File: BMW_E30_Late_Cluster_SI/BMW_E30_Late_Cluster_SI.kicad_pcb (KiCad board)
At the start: 2 copper layers, 78.7 x 3.1 mm, 12 parts, among them J1 SI LED Board, J5 Nexus Connector, Y1 Crystal, Y2 Crystal

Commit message: SI Board Cuts
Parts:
- moved J5 116.7 mm to (221.5, 133.5)
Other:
- board size 78.7 x 3.1 mm -> 300 x 53 mm
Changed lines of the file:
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@@
 	(footprint "BMW_Cluster_Connectors:E30_SI_Connector_Late_19Pin_P3.5"
 		(layer "F.Cu")
-		(at 272.5 28.5)
+		(at 221.5 133.5)
 		(property "Reference" "J5"
 			(at 35.835 3.875 0)
@@
 		)
 	)
+	(gr_line
+		(start 149.4 183)
+		(end 70 183)
+		(stroke
+			(width 0.05)
+			(type solid)
+		)
+		(layer "Edge.Cuts")
+	)
+	(gr_line
+		(start 70 130)
+		(end 70 183)
+		(stroke
+			(width 0.05)
+			(type default)
+		)
+		(layer "Edge.Cuts")
+	)
+	(gr_line
+		(start 289.4 175.7)
+		(end 264.5 175.7)
+		(stroke
+			(width 0.05)
+			(type solid)
+		)
+		(layer "Edge.Cuts")
+	)
+	(gr_line
+		(start 342 155.5)
+		(end 317 155.5)
+		(stroke
+			(width 0.05)
+			(type solid)
+		)
+		(layer "Edge.Cuts")
+	)
+	(gr_line
+		(start 70 130)
+		(end 370 130)
+		(stroke
+			(width 0.05)
+			(type solid)
+		)
+		(layer "Edge.Cuts")
+	)
+	(gr_line
+		(start 174.3 183)
+		(end 174.3 175.7)
+		(stroke
+			(width 0.05)
+			(type solid)
+		)
+		(layer "Edge.Cuts")
+	)
+	(gr_line
+		(start 264.5 183)
+		(end 174.3 183)
+		(stroke
+			(width 0.05)
+			(type solid)
+		)
+		(layer "Edge.Cuts")
+	)
+	(gr_line
+		(start 370 146.9)
+		(end 342 146.9)
+		(stroke
+			(width 0.05)
+			(type solid)
+		)
+		(layer "Edge.Cuts")
+	)
+	(gr_line
+		(start 149.4 183)
+		(end 149.4 175.7)
+		(stroke
+			(width 0.05)
+			(type solid)
+		)
+		(layer "Edge.Cuts")
+	)
+	(gr_line
+		(start 289.4 183)
+		(end 289.4 175.7)
+		(stroke
+			(width 0.05)
+			(type solid)
+		)
+		(layer "Edge.Cuts")
+	)
+	(gr_line
+		(start 370 130)
+		(end 370 146.9)
+		(stroke
+			(width 0.05)
+			(type solid)
+		)
+		(layer "Edge.Cuts")
+	)
+	(gr_line
+		(start 264.5 183)
+		(end 264.5 175.7)
+		(stroke
+			(width 0.05)
+			(type solid)
+		)
+		(layer "Edge.Cuts")
+	)
+	(gr_line
+		(start 310.1 179.2)
+		(end 306.1 179.2)
+		(stroke
+			(width 0.05)
+			(type solid)
+		)
+		(layer "Edge.Cuts")
+	)
+	(gr_line
+		(start 306.1 183)
+		(end 289.4 183)
+		(stroke
+			(width 0.05)
+			(type solid)
+		)
+		(layer "Edge.Cuts")
+	)
+	(gr_line
+		(start 310.1 146.9)
+		(end 310.1 179.2)
+		(stroke
+			(width 0.05)
+			(type solid)
+		)
+		(layer "Edge.Cuts")
+	)
+	(gr_line
+		(start 342 146.9)
+		(end 342 155.5)
+		(stroke
+			(width 0.05)
+			(type default)
+		)
+		(layer "Edge.Cuts")
+	)
+	(gr_line
+		(start 317 146.9)
+		(end 317 155.5)
+		(stroke
+			(width 0.05)
+			(type default)
+		)
+		(layer "Edge.Cuts")
+	)
+	(gr_line
+		(start 174.3 175.7)
+		(end 149.4 175.7)
+		(stroke
+			(width 0.05)
+			(type solid)
+		)
+		(layer "Edge.Cuts")
+	)
+	(gr_line
+		(start 306.1 179.2)
+		(end 306.1 183)
+		(stroke
+			(width 0.05)
+			(type solid)
+		)
+		(layer "Edge.Cuts")
+	)
+	(gr_line
+		(start 317 146.9)
+		(end 310.1 146.9)
+		(stroke
+			(width 0.05)
+			(type solid)
+		)
+		(layer "Edge.Cuts")
+	)
 	(embedded_fonts no)

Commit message: SI layout updates
Component positions are mostly complete.
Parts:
- added BT1: 3V, SI_THT:Batt_CR14250SE, F.Cu at (236.5, 155.9)
- added BT2: 3V, SI_THT:Batt_CR14250SE, F.Cu at (236.5, 142.3)
- added C1: 0.1u, Capacitor_THT:C_Disc_D6.0mm_W2.5mm_P5.00mm, F.Cu at (281.9, 114.3)
- added C10: 68n, Capacitor_THT:C_Disc_D6.0mm_W2.5mm_P5.00mm, F.Cu at (272.4, 120.2)
- added C13: 47u, Capacitor_THT:CP_Radial_Tantal_D9.0mm_P2.50mm, F.Cu at (90.1, 175.8)
- added C14: 10n, Capacitor_THT:C_Disc_D6.0mm_W2.5mm_P5.00mm, F.Cu at (127.7, 179.9)
- added C17: 68n, Capacitor_THT:C_Disc_D6.0mm_W2.5mm_P5.00mm, F.Cu at (163.3, 164.6)
- added C18: 0.1u, Capacitor_THT:C_Rect_L7.0mm_W2.0mm_P5.00mm, F.Cu at (219.5, 141.4)
- added C19: 0.1n, Capacitor_THT:C_Disc_D6.0mm_W2.5mm_P5.00mm, F.Cu at (210.6, 149.3)
- added C20: 0.1n, Capacitor_THT:C_Disc_D6.0mm_W2.5mm_P5.00mm, F.Cu at (219.8, 146.1)
- added C21: 0.1n, Capacitor_THT:C_Disc_D6.0mm_W2.5mm_P5.00mm, F.Cu at (85.0, 156.5)
- added C3: 0.1u, Capacitor_THT:C_Disc_D6.0mm_W2.5mm_P5.00mm, F.Cu at (281.9, 118.3)
- added C5: 0.1u, Capacitor_THT:C_Rect_L7.0mm_W2.0mm_P5.00mm, F.Cu at (293.9, 153.7)
- added C6: 0.033u, Capacitor_THT:C_Rect_L7.0mm_W2.0mm_P5.00mm, F.Cu at (238.7, 52.4)
- added C7: 10n, Capacitor_THT:C_Rect_L7.0mm_W2.0mm_P5.00mm, F.Cu at (238.7, 55.9)
- added C8: 47n, Capacitor_THT:C_Disc_D6.0mm_W2.5mm_P5.00mm, F.Cu at (272.4, 116.1)
- added C9: 68n, Capacitor_THT:C_Disc_D6.0mm_W2.5mm_P5.00mm, F.Cu at (281.9, 122.4)
- added D1: 1N4004, SI_THT:D_Axial_Narrow_L6.7mm_D2.4mm_P9.7mm, F.Cu at (262.0, 160.3)
- added D10: BZX55C-5V1, SI_THT:D_Axial_Narrow_L6.7mm_D2.4mm_P9.7mm, F.Cu at (187.2, 43.5)
- added D16: BZX55C-9V1, SI_THT:D_Axial_Narrow_L6.7mm_D2.4mm_P9.7mm, F.Cu at (79.6, 170.6)
- added D18: 1N4148, SI_THT:D_Axial_Narrow_L6.7mm_D2.4mm_P9.7mm, F.Cu at (187.2, 103.1)
- added D2: BAV21, SI_THT:D_Axial_Narrow_L6.7mm_D2.4mm_P9.7mm, F.Cu at (254.7, 41.9)
- added D24: SD103A, SI_THT:D_Axial_Narrow_L6.7mm_D2.4mm_P9.7mm, F.Cu at (214.3, 146.1)
- added D25: SD103A, SI_THT:D_Axial_Narrow_L6.7mm_D2.4mm_P9.7mm, F.Cu at (216.8, 146.1)
- added D26: LED, LED_THT:LED_D3.0mm, F.Cu at (90.7, 156.6)
- added D3: BAV21, SI_THT:D_Axial_Narrow_L6.7mm_D2.4mm_P9.7mm, F.Cu at (254.7, 45.5)
- added D4: 1N4004, SI_THT:D_Axial_Narrow_L6.7mm_D2.4mm_P9.7mm, F.Cu at (254.7, 49.1)
- added D5: BZX55C-5V1, SI_THT:D_Axial_Narrow_L6.7mm_D2.4mm_P9.7mm, F.Cu at (187.2, 32.7)
- added D6: BAV21, SI_THT:D_Axial_Narrow_L6.7mm_D2.4mm_P9.7mm, F.Cu at (94.6, 132.2)
- added D7: BZX55C-4V7, SI_THT:D_Axial_Narrow_L6.7mm_D2.4mm_P9.7mm, F.Cu at (87.1, 141.9)
- added D8: ZW 4.7, SI_THT:D_Axial_Narrow_L6.7mm_D2.4mm_P9.7mm, F.Cu at (245.7, 71.0)
- added D9: BAV21, SI_THT:D_Axial_Narrow_L6.7mm_D2.4mm_P9.7mm, F.Cu at (97.1, 141.9)
- added J2: Coding Plug, Connector_PinSocket_2.54mm:PinSocket_1x08_P2.54mm_Horizontal, F.Cu at (320.7, 142.1)
- added JP1: Battery Jumper, Connector_PinHeader_2.54mm:PinHeader_1x03_P2.54mm_Vertical, F.Cu at (206.0, 153.5)
- added Q11: BC327-16, Package_TO_SOT_THT:TO-92_Inline_Wide, F.Cu at (74.6, 146.4)
- added Q12: BC337-25, Package_TO_SOT_THT:TO-92_Inline_Wide, F.Cu at (79.6, 146.4)
- added Q13: BC337-16, Package_TO_SOT_THT:TO-92_Inline_Wide, F.Cu at (261.8, 136.0)
- added Q14: BC547B, Package_TO_SOT_THT:TO-92_Inline_Wide, F.Cu at (107.0, 176.7)
- added Q15: BC557B, Package_TO_SOT_THT:TO-92_Inline_Wide, F.Cu at (74.6, 173.1)
- added Q17: BC337-25, Package_TO_SOT_THT:TO-92_Inline_Wide, F.Cu at (79.6, 173.1)
- added Q19: BC337-25, Package_TO_SOT_THT:TO-92_Inline_Wide, F.Cu at (269.2, 168.2)
- added Q21: BC337-25, Package_TO_SOT_THT:TO-92_Inline_Wide, F.Cu at (261.5, 171.1)
- added Q22: BC337-25, Package_TO_SOT_THT:TO-92_Inline_Wide, F.Cu at (251.9, 171.1)
- added Q23: BC337-25, Package_TO_SOT_THT:TO-92_Inline_Wide, F.Cu at (256.7, 171.1)
- added R1: 2R2, SI_THT:R_Axial_Narrow_L6.8mm_D2.4mm_P9.7mm, F.Cu at (187.2, 47.1)
- added R10: 2k2, SI_THT:R_Axial_Narrow_L6.8mm_D2.4mm_P9.7mm, F.Cu at (82.1, 132.2)
- added R11: 2k21, SI_THT:R_Axial_Narrow_L6.8mm_D2.4mm_P9.7mm, F.Cu at (187.2, 65.1)
- added R12: 10k, SI_THT:R_Axial_Narrow_L6.8mm_D2.4mm_P9.7mm, F.Cu at (187.2, 68.7)
- added R13: 27k4, SI_THT:R_Axial_Narrow_L6.8mm_D2.4mm_P9.7mm, F.Cu at (187.2, 72.3)
- added R14: 47k, SI_THT:R_Axial_Narrow_L6.8mm_D2.4mm_P9.7mm, F.Cu at (92.1, 132.2)
- added R15: 47k, SI_THT:R_Axial_Narrow_L6.8mm_D2.4mm_P9.7mm, F.Cu at (89.6, 132.2)
- added R16: 1k5, SI_THT:R_Axial_Narrow_L6.8mm_D2.4mm_P9.7mm, F.Cu at (250.1, 114.5)
- added R17: 27k, SI_THT:R_Axial_Narrow_L6.8mm_D2.4mm_P9.7mm, F.Cu at (245.7, 96.2)
- added R18: 1k5, SI_THT:R_Axial_Narrow_L6.8mm_D2.4mm_P9.7mm, F.Cu at (245.7, 99.8)
- added R19: 470, SI_THT:R_Axial_Narrow_L6.8mm_D2.4mm_P9.7mm, F.Cu at (187.2, 83.1)
- added R2: 15k, SI_THT:R_Axial_Narrow_L6.8mm_D2.4mm_P9.7mm, F.Cu at (187.2, 50.7)
- added R21: 10k, SI_THT:R_Axial_Narrow_L6.8mm_D2.4mm_P9.7mm, F.Cu at (87.1, 160.8)
- added R22: 16k, SI_THT:R_Axial_Narrow_L6.8mm_D2.4mm_P9.7mm, F.Cu at (92.1, 160.8)
- added R23: 39k, SI_THT:R_Axial_Narrow_L6.8mm_D2.4mm_P9.7mm, F.Cu at (77.1, 160.8)
- added R24: 51k, SI_THT:R_Axial_Narrow_L6.8mm_D2.4mm_P9.7mm, F.Cu at (84.6, 160.8)
- added R25: 100R, SI_THT:R_Axial_Narrow_L6.8mm_D2.4mm_P9.7mm, F.Cu at (89.6, 170.6)
- added R26: 1k, SI_THT:R_Axial_Narrow_L6.8mm_D2.4mm_P9.7mm, F.Cu at (74.6, 170.6)
- added R28: 200R, SI_THT:R_Axial_Narrow_L6.8mm_D2.4mm_P9.7mm, F.Cu at (82.1, 170.6)
- added R29: 100k, SI_THT:R_Axial_Narrow_L6.8mm_D2.4mm_P9.7mm, F.Cu at (187.2, 113.9)
- added R3: 2R2, SI_THT:R_Axial_Narrow_L6.8mm_D2.4mm_P9.7mm, F.Cu at (187.2, 54.3)
- added R30: 75R, SI_THT:R_Axial_Narrow_L6.8mm_D2.4mm_P9.7mm, F.Cu at (187.2, 117.5)
- added R32: 160R, SI_THT:R_Axial_Narrow_L6.8mm_D2.4mm_P9.7mm, F.Cu at (188.2, 171.2)
- added R33: 160R, SI_THT:R_Axial_Narrow_L6.8mm_D2.4mm_P9.7mm, F.Cu at (190.7, 171.2)
- added R34: 160R, SI_THT:R_Axial_Narrow_L6.8mm_D2.4mm_P9.7mm, F.Cu at (193.2, 171.2)
- added R35: 160R, SI_THT:R_Axial_Narrow_L6.8mm_D2.4mm_P9.7mm, F.Cu at (200.7, 171.2)
- added R36: 160R, SI_THT:R_Axial_Narrow_L6.8mm_D2.4mm_P9.7mm, F.Cu at (198.2, 171.2)
- added R37: 160R, SI_THT:R_Axial_Narrow_L6.8mm_D2.4mm_P9.7mm, F.Cu at (203.2, 171.2)
- added R38: 160R, SI_THT:R_Axial_Narrow_L6.8mm_D2.4mm_P9.7mm, F.Cu at (205.7, 171.2)
- added R39: 4k7, SI_THT:R_Axial_Narrow_L6.8mm_D2.4mm_P9.7mm, F.Cu at (239.0, 180.8)
- added R4: 6k8, SI_THT:R_Axial_Narrow_L6.8mm_D2.4mm_P9.7mm, F.Cu at (74.6, 141.9)
- added R40: 4k7, SI_THT:R_Axial_Narrow_L6.8mm_D2.4mm_P9.7mm, F.Cu at (241.5, 180.8)
- added R41: 4k7, SI_THT:R_Axial_Narrow_L6.8mm_D2.4mm_P9.7mm, F.Cu at (247.4, 180.8)
- added R42: 82R, SI_THT:R_Axial_Narrow_L6.8mm_D2.4mm_P9.7mm, F.Cu at (196.4, 139.6)
- added R43: 82R, SI_THT:R_Axial_Narrow_L6.8mm_D2.4mm_P9.7mm, F.Cu at (193.9, 139.6)
- added R44: 2k, SI_THT:R_Axial_Narrow_L6.8mm_D2.4mm_P9.7mm, F.Cu at (162.1, 142.8)
- added R45: 1M, SI_THT:R_Axial_Narrow_L6.8mm_D2.4mm_P9.7mm, F.Cu at (180.6, 164.5)
- added R46: 100R, SI_THT:R_Axial_Narrow_L6.8mm_D2.4mm_P9.7mm, F.Cu at (92.0, 153.0)
- added R5: 4k6, SI_THT:R_Axial_Narrow_L6.8mm_D2.4mm_P9.7mm, F.Cu at (77.1, 132.2)
- added R7: 27k, SI_THT:R_Axial_Narrow_L6.8mm_D2.4mm_P9.7mm, F.Cu at (187.2, 57.9)
- added R8: 3k92, SI_THT:R_Axial_Narrow_L6.8mm_D2.4mm_P9.7mm, F.Cu at (187.2, 61.5)
- added R9: 4k6, SI_THT:R_Axial_Narrow_L6.8mm_D2.4mm_P9.7mm, F.Cu at (79.6, 132.2)
- added U1: ITT SAF1190-196 MCU, Package_DIP:DIP-40_W15.24mm_LongPads, F.Cu at (99.8, 151.4)
- added U2: ITT V3003-393, Package_DIP:DIP-18_W7.62mm_LongPads, F.Cu at (175.9, 132.6)
- added U3: ITT V3004-520, Package_DIP:DIP-24_W15.24mm_LongPads, F.Cu at (163.3, 160.7)
- added U4: ITT SAF1194-280 MCU, Package_DIP:DIP-40_W15.24mm_LongPads, F.Cu at (99.8, 171.1)
- added U5: LP2950-5.0_TO92, Package_TO_SOT_THT:TO-92_Inline_Wide, F.Cu at (292.1, 142.9)
- J5: footprint BMW_Cluster_Connectors:E30_SI_Connector_Late_19Pin_P3.5 -> BMW_Cluster_Connectors:E30_Early_SI_Conn_Late_P3.5
- moved C11 282.1 mm to (100.1, 176.5), turned to -90 degrees
- moved Y2 278.5 mm to (115.0, 176.4), turned to 90 degrees
- moved R20 195.5 mm to (151.2, 162.7), turned to 90 degrees
- moved Y1 194.6 mm to (195.8, 161.9), turned to 90 degrees
- moved C12 156.8 mm to (209.9, 175.8)
- moved C15 144.4 mm to (302.9, 140.2)
- moved R6 138.6 mm to (298.7, 132.9)
- moved J1 131.4 mm to (234.6, 168.6), turned to -90 degrees
- moved C4 119.2 mm to (274.8, 170.9)
- moved R27 94.6 mm to (304.2, 155.7), turned to -90 degrees
- moved C2 86.6 mm to (294.5, 136.0), turned to 180 degrees
- moved J5 1.50 mm to (220.6, 132.3)
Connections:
- C11 pad 1: unconnected-(C11-Pad1) -> Net-(C11-Pad1)
- C11 pad 2: unconnected-(C11-Pad2) -> GNDPWR
- C12 pad 1: unconnected-(C12-Pad1) -> Net-(Q17-C)
- C12 pad 2: unconnected-(C12-Pad2) -> GNDPWR
- C15 pad 1: unconnected-(C15-Pad1) -> +5V
- C15 pad 2: unconnected-(C15-Pad2) -> GNDPWR
- C2 pad 1: unconnected-(C2-Pad1) -> VCC_T30
- C2 pad 2: unconnected-(C2-Pad2) -> GNDPWR
- C4 pad 1: unconnected-(C4-Pad1) -> VCC_T15
- C4 pad 2: unconnected-(C4-Pad2) -> GNDPWR
- J1 pad 1: unconnected-(J1-Pin_1-Pad1) -> VCC_T15
- J1 pad 10: unconnected-(J1-Pin_10-Pad10) -> Net-(J1-Pin_10)
- J1 pad 11: unconnected-(J1-Pin_11-Pad11) -> Net-(J1-Pin_11)
- J1 pad 12: unconnected-(J1-Pin_12-Pad12) -> Net-(J1-Pin_12)
- J1 pad 2: unconnected-(J1-Pin_2-Pad2) -> Net-(J1-Pin_2)
- J1 pad 3: unconnected-(J1-Pin_3-Pad3) -> Net-(J1-Pin_3)
- J1 pad 4: unconnected-(J1-Pin_4-Pad4) -> Net-(J1-Pin_4)
- J1 pad 5: unconnected-(J1-Pin_5-Pad5) -> Net-(J1-Pin_5)
- J1 pad 6: unconnected-(J1-Pin_6-Pad6) -> Net-(J1-Pin_6)
- J1 pad 7: unconnected-(J1-Pin_7-Pad7) -> Net-(J1-Pin_7)
- J1 pad 8: unconnected-(J1-Pin_8-Pad8) -> Net-(J1-Pin_8)
- J1 pad 9: unconnected-(J1-Pin_9-Pad9) -> Net-(J1-Pin_9)
- R20 pad 1: unconnected-(R20-Pad1) -> IC3_P7
- R20 pad 2: unconnected-(R20-Pad2) -> IC1_P23
- R27 pad 1: unconnected-(R27-Pad1) -> T30_Protected
- R27 pad 2: unconnected-(R27-Pad2) -> Net-(Q17-C)
- R6 pad 2: unconnected-(R6-Pad2) -> Net-(Q11-C)
- Y1 pad 1: unconnected-(Y1-Pad1) -> IC2_P12
- Y1 pad 2: unconnected-(Y1-Pad2) -> IC2_P11
- Y2 pad 1: unconnected-(Y2-Pad1) -> Net-(U4-Pad6)
- Y2 pad 2: unconnected-(Y2-Pad2) -> Net-(U4-Pad7)
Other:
- outline, holes or cut-outs redrawn

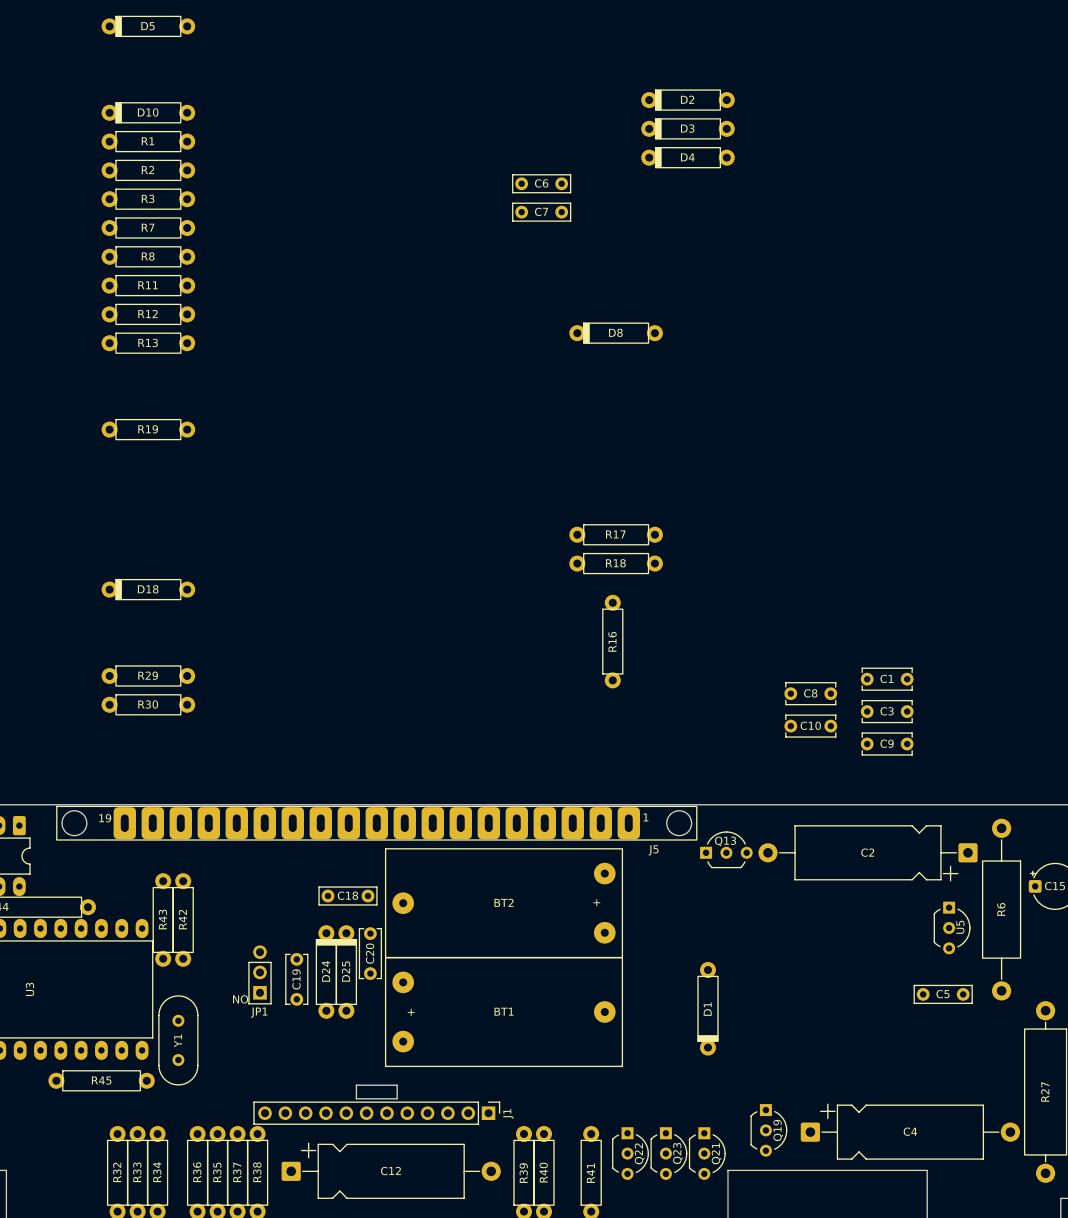
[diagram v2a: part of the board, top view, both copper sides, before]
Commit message: Component Locations Generally Set
Component locations set up and ready for layout to begin.
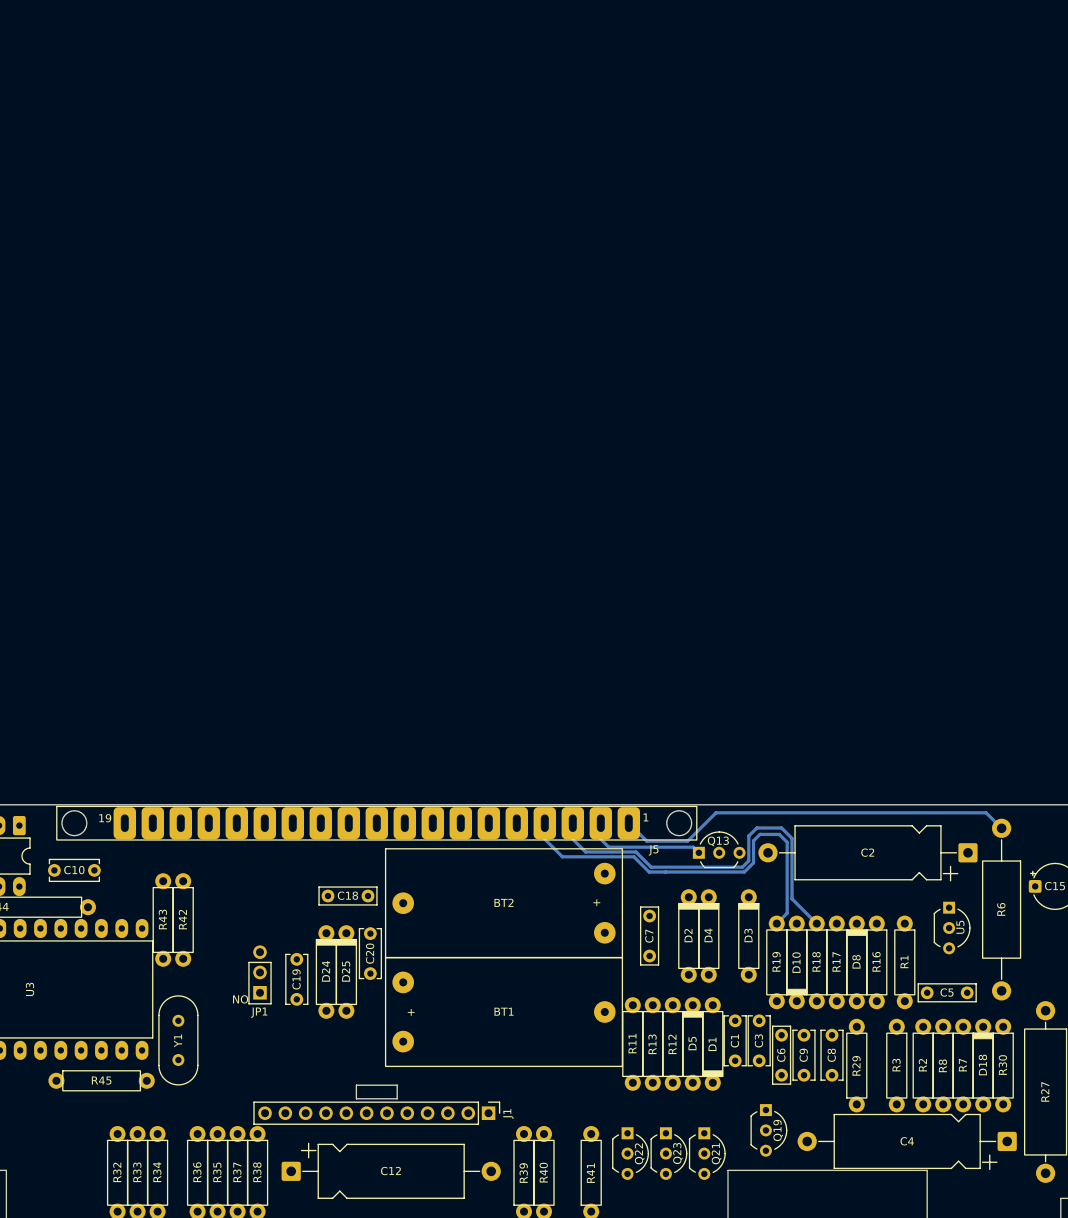
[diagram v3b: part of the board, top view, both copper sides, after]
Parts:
- moved R8 148.6 mm to (291.4, 167.4), turned to 90 degrees
- moved R2 147.7 mm to (288.9, 157.8), turned to -90 degrees
- moved R7 146.1 mm to (293.9, 157.8), turned to -90 degrees
- moved R3 142.8 mm to (285.6, 157.8), turned to -90 degrees
- moved D5 142.4 mm to (260.1, 155.1), turned to -90 degrees
- moved D10 140.4 mm to (273.1, 154.6), turned to 90 degrees
- moved R1 139.4 mm to (286.6, 144.8), turned to -90 degrees
- moved D18 122.1 mm to (296.4, 157.8), turned to -90 degrees
- moved R12 119.1 mm to (257.6, 164.8), turned to 90 degrees
- moved R30 118.7 mm to (298.9, 157.8), turned to -90 degrees
- moved R13 114.7 mm to (255.1, 164.8), turned to 90 degrees
- moved C6 111.3 mm to (271.2, 158.8), turned to -90 degrees
- moved R11 111.2 mm to (252.6, 155.1), turned to -90 degrees
- moved R29 107.7 mm to (280.6, 167.4), turned to 90 degrees
- moved R19 103.8 mm to (270.6, 144.8), turned to -90 degrees
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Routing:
- net Temp_+Ub: track 0.00 -> 49.8 mm
- net SI_RST: track 0.00 -> 48.7 mm
- net Eng_temp_sensor: track 0.00 -> 47.2 mm
- net Temp_GND: track 0.00 -> 15.0 mm

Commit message: SI Board Layout Updates
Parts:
- moved U5 1.34 mm to (290.8, 142.9)
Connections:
- net T30_Protected renamed Net-(D1-K)
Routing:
- net Net-(Q11-C): track 0.00 -> 273.5 mm, vias 0 -> 1
- net Net-(Q13-B): track 0.00 -> 235.4 mm, vias 0 -> 1
- net GNDPWR: track 0.00 -> 196.2 mm
- net +5V: track 0.00 -> 104.1 mm, vias 0 -> 2
- net Net-(Q19-C): track 0.00 -> 102.9 mm
- net Net-(D1-K): track 0.00 -> 68.0 mm
- net +12_T30: track 0.00 -> 62.6 mm, vias 0 -> 2
- net +12_T15: track 0.00 -> 56.2 mm, vias 0 -> 2
- net Net-(D2-K): track 0.00 -> 42.7 mm
- net Net-(Q17-C): track 0.00 -> 42.0 mm
- net IGN_Check: track 0.00 -> 41.1 mm, vias 0 -> 2
- net VCC_T15: track 0.00 -> 20.8 mm, vias 0 -> 1
- net VCC_T30: track 0.00 -> 20.4 mm
- net Net-(D5-A): track 0.00 -> 15.8 mm
- net IC1_P22: track 0.00 -> 9.85 mm
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- added copper zone on B.Cu, net GNDPWR

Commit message: SI Board Layout Updates
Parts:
- R20: footprint Resistor_THT:R_Axial_DIN0207_L6.3mm_D2.5mm_P15.24mm_Horizontal -> SI_THT:R_Axial_DIN0207_L6.3mm_D2.5mm_P22.2mm_Horizontal
- R44: footprint SI_THT:R_Axial_Narrow_L6.8mm_D2.4mm_P9.7mm -> SI_THT:R_Axial_Narrow_L6.8mm_D2.4mm_P22.4mm
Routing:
- net VCC_T15: track 20.8 -> 413.6 mm, vias 1 -> 3
- net IC1_P17: track 0.00 -> 87.6 mm, vias 0 -> 1
- net Net-(C14-Pad1): track 0.00 -> 73.3 mm, vias 0 -> 1
- net Net-(C6-Pad1): track 0.00 -> 21.1 mm
- net GNDPWR: track 196.2 -> 215.9 mm, vias 0 -> 1
- net IC1_P19: track 0.00 -> 11.6 mm, vias 0 -> 1
- net IC4_P40: track 0.00 -> 7.12 mm
- net Net-(R2-Pad2): track 0.00 -> 5.00 mm

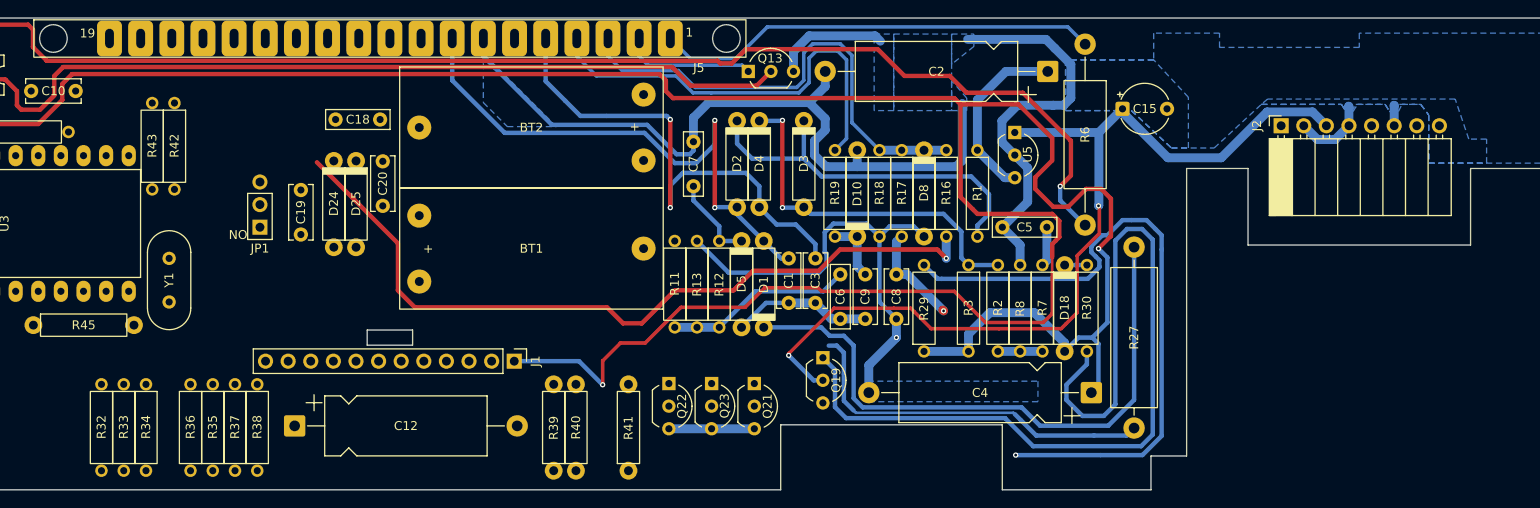
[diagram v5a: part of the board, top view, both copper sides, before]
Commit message: SI Board Layout Updates
Continued updating traces from the coding plug side of the board.
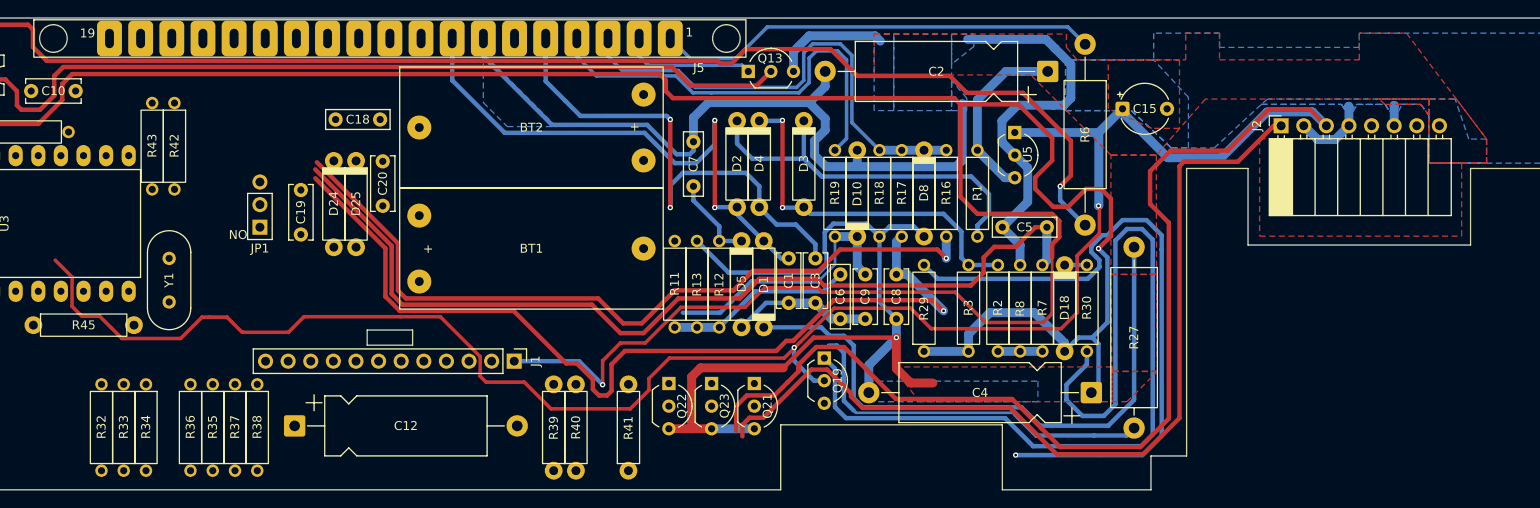
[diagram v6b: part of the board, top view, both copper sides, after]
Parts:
- moved Q19 0.16 mm to (269.4, 168.2)
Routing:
- net +5V: track 104.1 -> 316.7 mm
- net IC1_P2: track 0.00 -> 100.4 mm
- net IC1_P20: track 4.46 -> 104.0 mm
- net IC1_P19: track 11.6 -> 102.7 mm
- net GNDPWR: track 215.9 -> 254.8 mm
- net IC4_P40: track 7.12 -> 29.6 mm
- added copper zone on F.Cu, net GNDPWR

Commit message: SI Board Layout Updates
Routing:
- net Net-(C14-Pad1): track 73.3 -> 305.3 mm, vias 1 -> 3
- net IC1_P4: track 0.00 -> 144.1 mm
- net IC1_P3: track 0.00 -> 140.3 mm
- net +5V: track 316.7 -> 204.1 mm
- net Net-(Q17-C): track 42.0 -> 127.4 mm, vias 0 -> 1
- net Net-(D1-K): track 68.0 -> 130.9 mm, vias 0 -> 1
- net Net-(J1-Pin_11): track 0.00 -> 62.3 mm
- net Net-(J1-Pin_10): track 0.00 -> 51.2 mm
- net Net-(J1-Pin_2): track 0.00 -> 49.9 mm
- net Net-(J1-Pin_9): track 0.00 -> 44.7 mm
- net Net-(Q21-B): track 0.00 -> 37.6 mm
- net IC4_P40: track 29.6 -> 65.2 mm, vias 0 -> 1
- net IC1_P2: track 100.4 -> 124.5 mm
- net Net-(Q22-B): track 0.00 -> 11.5 mm
- net Net-(Q23-B): track 0.00 -> 11.4 mm
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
